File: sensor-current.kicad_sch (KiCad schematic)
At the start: 0 parts

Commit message: Adding I2C bus to circuit
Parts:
- added U8: INA260, Package_SO:TSSOP-16_4.4x5mm_P0.65mm, symbol Sensor:INA260
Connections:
- new net: U8.1 (IN+), U8.2 (IN+), U8.3 (IN+)
- new net: U8.14 (IN-), U8.15 (IN-), U8.16 (IN-)
- new net GND: U8.11 (GND), U8.6 (GND)
- new net I2C.SCL: U8.9 (SCL)
- new net I2C.SDA: U8.8 (SDA)
- no-connect marks 0 -> 3
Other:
- note added: "Where to connect the INA to? BATT VBUS lines"
- note added: "n/c"

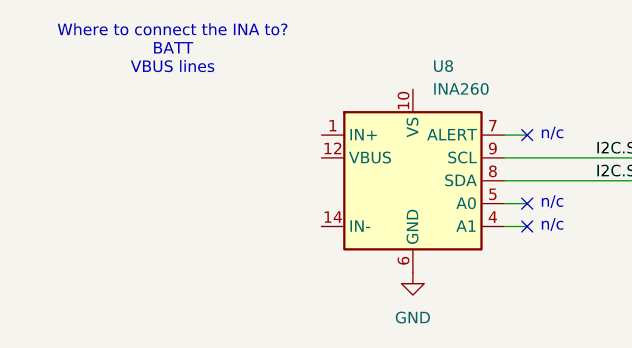
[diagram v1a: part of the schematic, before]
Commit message: Adding symbols information
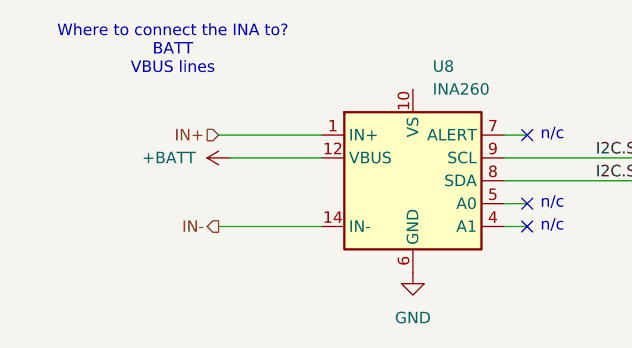
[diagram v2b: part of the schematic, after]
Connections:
- net IN+: now reaches U8.1 (IN+), U8.2 (IN+), U8.3 (IN+)
- net +BATT: now reaches U8.12 (VBUS)
- net IN-: now reaches U8.14 (IN-), U8.15 (IN-), U8.16 (IN-)
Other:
- company: (none) -> catbranchman
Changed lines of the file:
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@@
 	(generator_version "8.0")
 	(paper "A4")
+	(title_block
+		(company "catbranchman")
+		(comment 1 "Electrical Engineering Department")
+		(comment 2 "EE 156 / Stanford University")
+		(comment 3 "Flight Club, W6YX, Endurance")
+	)
 	(no_connect
 		(at 163.83 95.25)
@@
 		)
 	)
+	(wire
+		(pts
+			(xy 129.54 105.41) (xy 140.97 105.41)
+		)
+		(stroke
+			(width 0)
+			(type default)
+		)
+	)
 	(bus
 		(pts
@@
 	(wire
 		(pts
+			(xy 130.81 97.79) (xy 140.97 97.79)
+		)
+		(stroke
+			(width 0)
+			(type default)
+		)
+	)
+	(wire
+		(pts
 			(xy 161.29 95.25) (xy 163.83 95.25)
 		)
@@
 		(pts
 			(xy 161.29 105.41) (xy 163.83 105.41)
+		)
+		(stroke
+			(width 0)
+			(type default)
+		)
+	)
+	(wire
+		(pts
+			(xy 129.54 95.25) (xy 140.97 95.25)
 		)
 		(stroke
@@
 		)
 	)
+	(hierarchical_label "IN-"
+		(shape output)
+		(at 129.54 105.41 180)
+		(fields_autoplaced yes)
+		(effects
+			(font
+				(size 1.27 1.27)
+			)
+			(justify right)
+		)
+	)
+	(hierarchical_label "IN+"
+		(shape input)
+		(at 129.54 95.25 180)
+		(fields_autoplaced yes)
+		(effects
+			(font
+				(size 1.27 1.27)
+			)
+			(justify right)
+		)
+	)
+	(symbol
+		(lib_id "power:+BATT")
+		(at 130.81 97.79 90)
+		(unit 1)
+		(exclude_from_sim no)
+		(in_bom yes)
+		(on_board yes)
+		(dnp no)
+		(fields_autoplaced yes)
+		(property "Reference" "#PWR053"
+			(at 134.62 97.79 0)
+			(effects
+				(font
+					(size 1.27 1.27)
+				)
+				(hide yes)
+			)
+		)
+		(property "Value" "+BATT"
+			(at 127 97.7899 90)
+			(effects
+				(font
+					(size 1.27 1.27)
+				)
+				(justify left)
+			)
+		)
+		(property "Footprint" ""
+			(at 130.81 97.79 0)
+			(effects
+				(font
+					(size 1.27 1.27)
+				)
+				(hide yes)
+			)
+		)
+		(property "Datasheet" ""
+			(at 130.81 97.79 0)
+			(effects
+				(font
+					(size 1.27 1.27)
+				)
+				(hide yes)
+			)
+		)
+		(property "Description" "Power symbol creates a global label with name \"+BATT\""
+			(at 130.81 97.79 0)
+			(effects
+				(font
+					(size 1.27 1.27)
+				)
+				(hide yes)
+			)
+		)
+		(pin "1"
+		)
+		(instances
+			(project "roamer"
+				(path "/1c59de6a-87fe-4223-8898-4b0383164a31/7697eacc-831c-4a5e-b109-0bbe6f3888c4"
+					(reference "#PWR053")
+					(unit 1)
+				)
+			)
+		)
+	)

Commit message: Adding rest of schematic
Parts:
- U8: Mfr (none) -> Texas Instruments; Mfr P/N (none) -> INA260AIPWR; Supplier_1 (none) -> Digikey; Supplier_1 P/N (none) -> 296-47777-1-ND; Supplier_1 Price @ Qty (none) -> $2.85475; Supplier_1 Unit Price (none) -> $5.43000
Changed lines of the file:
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@@
 			)
 		)
-		(property "Description" "Current/power/voltage monitor with Integrated 2mΩ Shunt Resistor, 2.7V - 5.5V, I2C, TSSOP-16"
+		(property "Description" "Current Monitor Regulator High/Low-Side 10mA 16-TSSOP"
 			(at 151.13 100.33 0)
 			(effects
+				(font
+					(size 1.27 1.27)
+				)
+				(hide yes)
+			)
+		)
+		(property "Mfr" "Texas Instruments"
+			(at 151.13 100.33 0)
+			(effects
+				(font
+					(size 1.27 1.27)
+				)
+				(hide yes)
+			)
+		)
+		(property "Mfr P/N" "INA260AIPWR"
+			(at 151.13 100.33 0)
+			(effects
+				(font
+					(size 1.27 1.27)
+				)
+				(hide yes)
+			)
+		)
+		(property "Supplier_1" "Digikey"
+			(at 151.13 100.33 0)
+			(effects
+				(font
+					(size 1.27 1.27)
+				)
+				(hide yes)
+			)
+		)
+		(property "Supplier_1 P/N" "296-47777-1-ND"
+			(at 151.13 100.33 0)
+			(effects
+				(font
+					(size 1.27 1.27)
+				)
+				(hide yes)
+			)
+		)
+		(property "Supplier_1 Unit Price" "$5.43000"
+			(at 151.13 100.33 0)
+			(effects
+				(font
+					(size 1.27 1.27)
+				)
+				(hide yes)
+			)
+		)
+		(property "Supplier_1 Price @ Qty" "$2.85475"
+			(at 151.13 100.33 0)
+			(effects
+				(font
+					(size 1.27 1.27)
+				)
+				(hide yes)
+			)
+		)
+		(property "Supplier_2" ""
+			(at 151.13 100.33 0)
+			(effects
+				(font
+					(size 1.27 1.27)
+				)
+				(hide yes)
+			)
+		)
+		(property "Supplier_2 P/N" ""
+			(at 151.13 100.33 0)
+			(effects
+				(font
+					(size 1.27 1.27)
+				)
+				(hide yes)
+			)
+		)
+		(property "Supplier_2 Unit Price" ""
+			(at 151.13 100.33 0)
+			(effects
+				(font
+					(size 1.27 1.27)
+				)
+				(hide yes)
+			)
+		)
+		(property "Supplier_2 Price @ Qty" ""
+			(at 151.13 100.33 0)
+			(effects

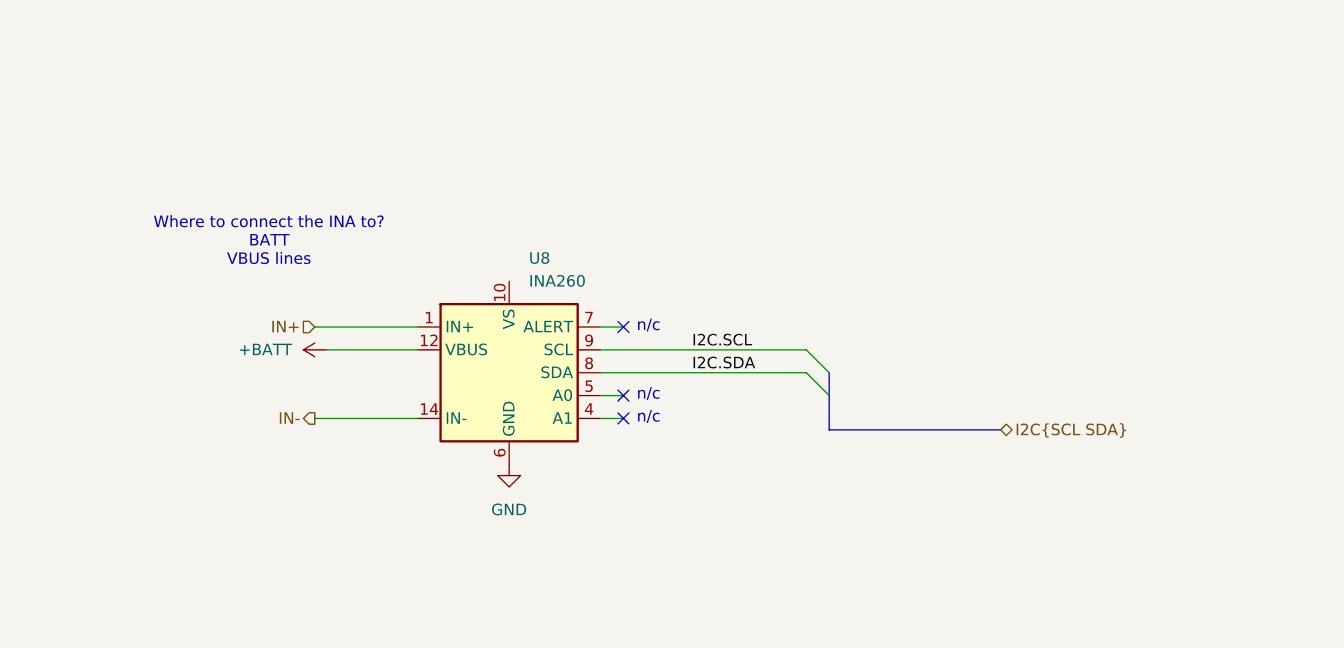
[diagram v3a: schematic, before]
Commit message: Spamming 0 ohm resistors
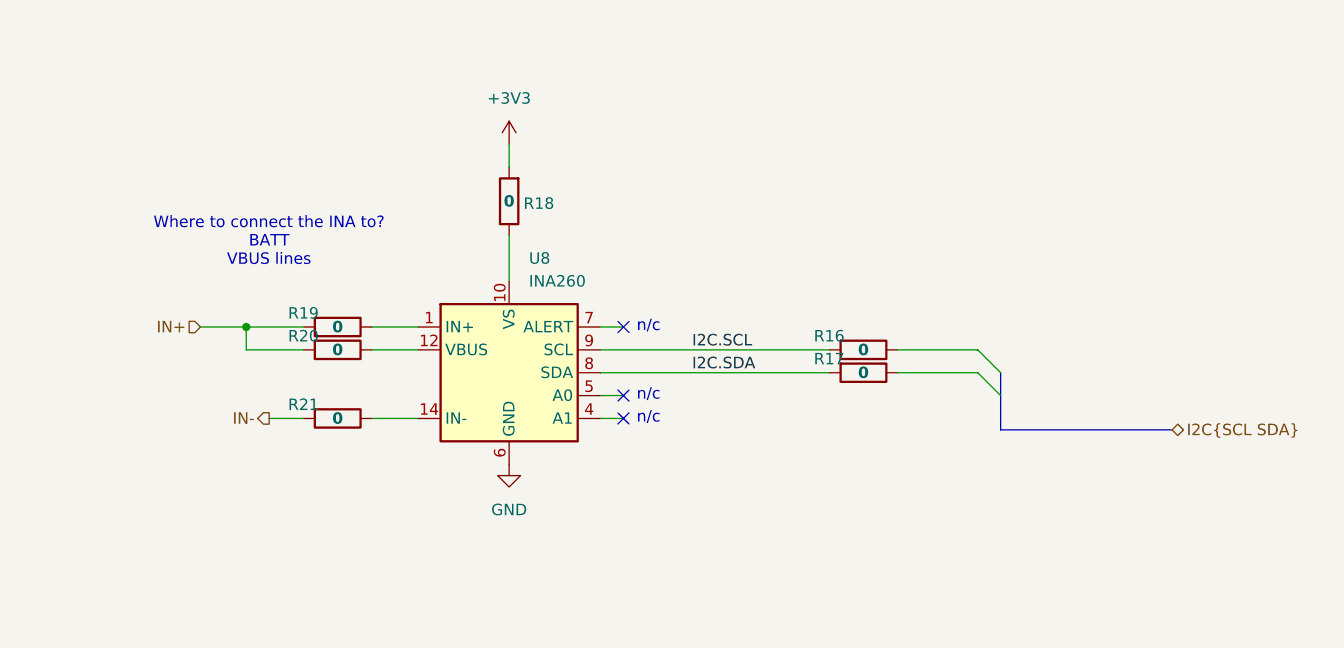
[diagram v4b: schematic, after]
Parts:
- added R16, R17, R18, R19, R20, R21: 0, Resistor_SMD:R_0603_1608Metric, symbol Device:R
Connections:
- net I2C.SCL: now also R16.2
- net I2C.SDA: now also R17.2
- net IN+: now also R19.2, R20.2; no longer U8.1 (IN+), U8.2 (IN+), U8.3 (IN+)
- net IN-: now also R21.2; no longer U8.14 (IN-), U8.15 (IN-), U8.16 (IN-)
- net at U8.10 (VS): now also R18.1
- net +BATT: no longer names the net of U8.12 (VBUS)
- net +BATT: now also R20.1
- new net: R19.1, U8.1 (IN+), U8.2 (IN+), U8.3 (IN+)
- new net: R21.1, U8.14 (IN-), U8.15 (IN-), U8.16 (IN-)
- new net +3V3: R18.2
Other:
- title: (none) -> Sensor - Current

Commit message: Adding more 0 ohm resistors and pullups for I2C lines
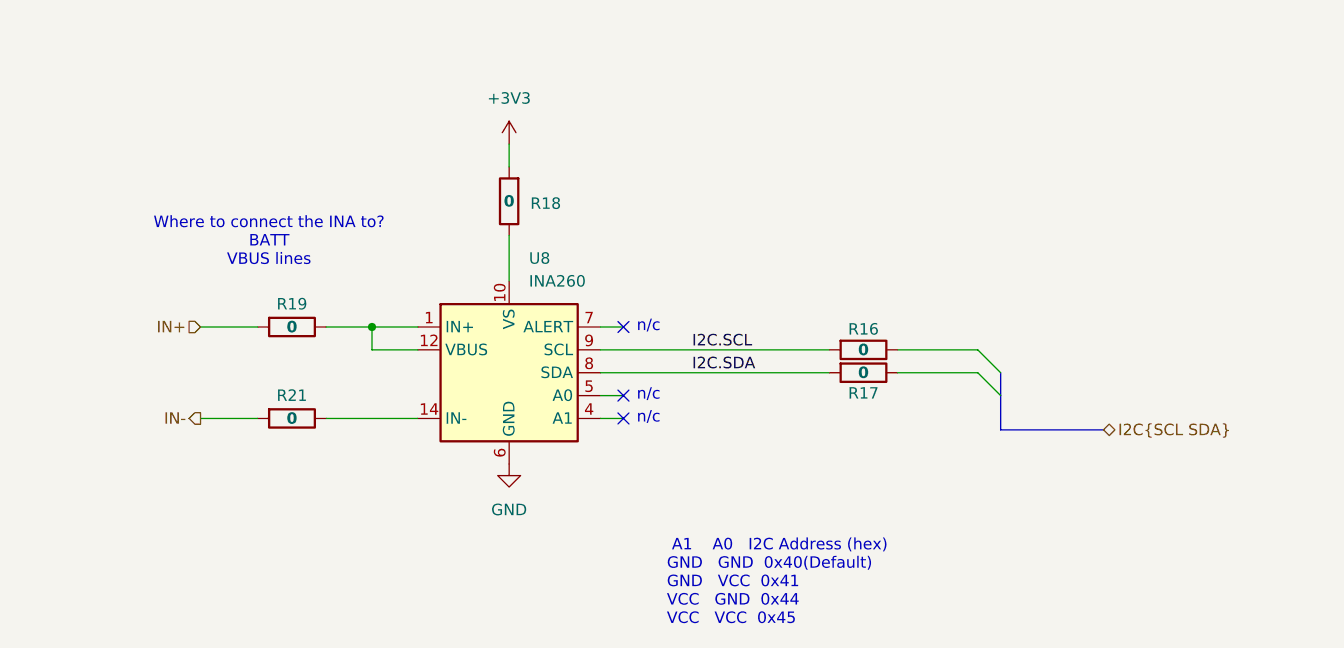
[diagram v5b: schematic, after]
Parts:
- removed R20: 0, Resistor_SMD:R_0603_1608Metric, symbol Device:R
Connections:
- net at R19.1, U8.1 (IN+), U8.2 (IN+)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: now also U8.12 (VBUS)
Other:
- note added: "A1 A0 I2C Address (hex) GND GND 0x40(Default) GND VCC 0x41 VCC GND 0x44 VCC VCC 0x45"
- moved on the sheet: R19, R21

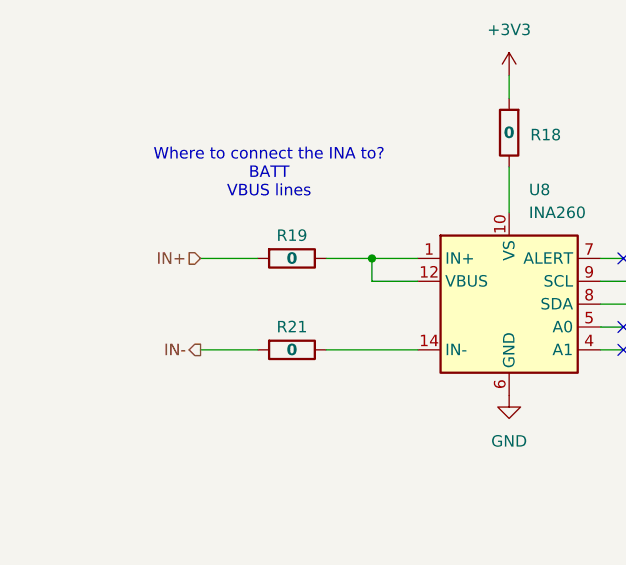
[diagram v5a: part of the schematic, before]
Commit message: Adding testpoints to I2C, SPI, and signals
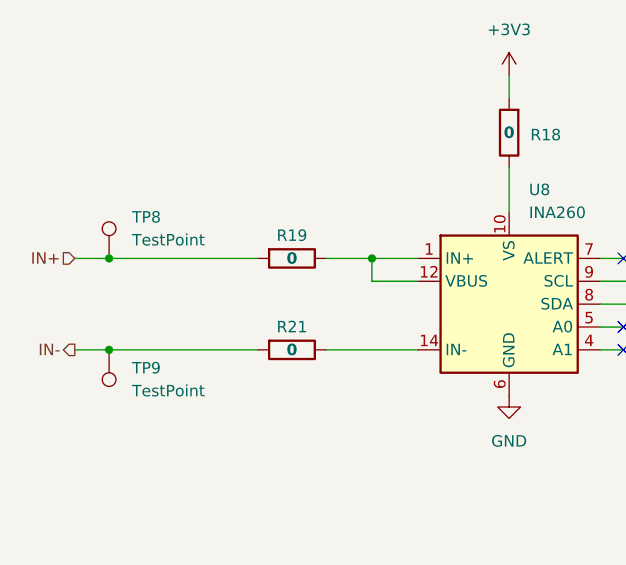
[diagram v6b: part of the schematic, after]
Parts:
- added TP8, TP9: TestPoint, TestPoint:TestPoint_Loop_D2.50mm_Drill1.0mm, symbol Connector:TestPoint
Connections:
- net IN+: now also TP8.1
- net IN-: now also TP9.1
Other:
- note removed: "Where to connect the INA to? BATT VBUS lines"

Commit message: Fixing lots of ERC errors
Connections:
- net I2C.SCL: now also R16.1; no longer R16.2, U8.9 (SCL)
- net I2C.SDA: now also R17.1; no longer R17.2, U8.8 (SDA)
- new net: R16.2, U8.9 (SCL)
- new net: R17.2, U8.8 (SDA)
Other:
- moved on the sheet: R16, R17
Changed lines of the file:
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@@
+	)
+	(junction
+		(at 151.13 87.63)
+		(diameter 0)
+		(color 0 0 0 0)
 	)
 	(junction
@@
 	)
 	(bus_entry
-		(at 203.2 97.79)
+		(at 191.77 97.79)
 		(size 2.54 2.54)
 		(stroke
@@
 	)
 	(bus_entry
-		(at 203.2 100.33)
+		(at 191.77 100.33)
 		(size 2.54 2.54)
 		(stroke
@@
 	(wire
 		(pts
-			(xy 151.13 85.09) (xy 151.13 90.17)
+			(xy 151.13 85.09) (xy 151.13 87.63)
 		)
 		(stroke
@@
 	(bus
 		(pts
-			(xy 205.74 100.33) (xy 205.74 102.87)
+			(xy 194.31 100.33) (xy 194.31 102.87)
 		)
 		(stroke
@@
 	(wire
 		(pts
-			(xy 194.31 100.33) (xy 203.2 100.33)
+			(xy 177.8 100.33) (xy 191.77 100.33)
 		)
 		(stroke
@@
 	(wire
 		(pts
-			(xy 161.29 100.33) (xy 186.69 100.33)
-		)
-		(stroke
-			(width 0)
-			(type default)
-		)
-	)
-	(wire
-		(pts
-			(xy 161.29 97.79) (xy 186.69 97.79)
+			(xy 161.29 100.33) (xy 170.18 100.33)
+		)
+		(stroke
+			(width 0)
+			(type default)
+		)
+	)
+	(wire
+		(pts
+			(xy 161.29 97.79) (xy 170.18 97.79)
 		)
 		(stroke
@@
 	(wire
 		(pts
-			(xy 194.31 97.79) (xy 203.2 97.79)
+			(xy 177.8 97.79) (xy 191.77 97.79)
 		)
 		(stroke
@@
 	(bus
 		(pts
-			(xy 205.74 102.87) (xy 205.74 106.68)
+			(xy 194.31 102.87) (xy 194.31 106.68)
+		)
+		(stroke
+			(width 0)
+			(type default)
+		)
+	)
+	(wire
+		(pts
+			(xy 151.13 87.63) (xy 151.13 90.17)
 		)
 		(stroke
@@
 	(bus
 		(pts
-			(xy 205.74 106.68) (xy 217.17 106.68)
+			(xy 194.31 106.68) (xy 205.74 106.68)
 		)
 		(stroke
@@
 	)
 	(label "I2C.SDA"
-		(at 171.45 100.33 0)
+		(at 180.34 100.33 0)
 		(fields_autoplaced yes)
 		(effects
@@
 	)
 	(label "I2C.SCL"
-		(at 171.45 97.79 0)
+		(at 180.34 97.79 0)
 		(fields_autoplaced yes)
 		(effects
@@
 	(hierarchical_label "I2C{SCL SDA}"
 		(shape bidirectional)
-		(at 217.17 106.68 0)
+		(at 205.74 106.68 0)
 		(fields_autoplaced yes)
 		(effects
@@
 	(symbol
 		(lib_id "Device:R")
-		(at 190.5 97.79 270)
+		(at 173.99 97.79 270)
 		(unit 1)
 		(exclude_from_sim no)
@@
 		(dnp no)
 		(property "Reference" "R16"
-			(at 190.5 95.504 90)
+			(at 173.99 95.504 90)
 			(effects
 				(font
@@
 		)
 		(property "Value" "0"
-			(at 190.5 97.79 90)
+			(at 173.99 97.79 90)
 			(effects
 				(font
@@
 		)
 		(property "Footprint" "Resistor_SMD:R_0603_1608Metric"
-			(at 190.5 96.012 90)
+			(at 173.99 96.012 90)
 			(effects
 				(font
@@
 		)
 		(property "Datasheet" "Datasheet"
-			(at 190.5 97.79 0)
+			(at 173.99 97.79 0)
 			(effects
 				(font
@@
 		)
 		(property "Description" "Resistor"
-			(at 190.5 97.79 0)
+			(at 173.99 97.79 0)
 			(effects
 				(font
@@
 		)
 		(property "Mfr" "YAGEO"
-			(at 190.5 97.79 0)
+			(at 173.99 97.79 0)
 			(effects
 				(font
@@
 		)
 		(property "Mfr P/N" "RC0603JR-070RL"
-			(at 190.5 97.79 0)
+			(at 173.99 97.79 0)
 			(effects
 				(font
@@
 		)
 		(property "Supplier_1" "Digikey"
-			(at 190.5 97.79 0)
+			(at 173.99 97.79 0)
 			(effects
 				(font
@@
 		)
 		(property "Supplier_1 P/N" "311-0.0GRCT-ND"
-			(at 190.5 97.79 0)
+			(at 173.99 97.79 0)
 			(effects
 				(font
@@
 		)
 		(property "Supplier_1 Unit Price" "$0.10000 "
-			(at 190.5 97.79 0)
+			(at 173.99 97.79 0)
 			(effects
 				(font
@@
 		)
 		(property "Supplier_1 Price @ Qty" "$0.00304 "
-			(at 190.5 97.79 0)
+			(at 173.99 97.79 0)
 			(effects
 				(font
@@
 		)
 		(property "Supplier_2" ""
-			(at 190.5 97.79 0)
+			(at 173.99 97.79 0)
 			(effects
 				(font
@@
 		)
 		(property "Supplier_2 P/N" ""
-			(at 190.5 97.79 0)
+			(at 173.99 97.79 0)
 			(effects
 				(font
@@
 		)
 		(property "Supplier_2 Unit Price" ""
-			(at 190.5 97.79 0)
+			(at 173.99 97.79 0)
 			(effects
 				(font
@@
 		)
 		(property "Supplier_2 Price @ Qty" ""
-			(at 190.5 97.79 0)
+			(at 173.99 97.79 0)
 			(effects
 				(font
@@
 	(symbol
 		(lib_id "Device:R")
-		(at 190.5 100.33 270)
+		(at 173.99 100.33 270)
 		(unit 1)
 		(exclude_from_sim no)
@@
 		(dnp no)
 		(property "Reference" "R17"
-			(at 190.5 102.616 90)
+			(at 173.99 102.616 90)
 			(effects
 				(font
@@
 		)
 		(property "Value" "0"
-			(at 190.5 100.33 90)
+			(at 173.99 100.33 90)
 			(effects
 				(font
@@
 		)
 		(property "Footprint" "Resistor_SMD:R_0603_1608Metric"
-			(at 190.5 98.552 90)
+			(at 173.99 98.552 90)
 			(effects
 				(font
@@
 		)
 		(property "Datasheet" "Datasheet"
-			(at 190.5 100.33 0)
+			(at 173.99 100.33 0)
 			(effects
 				(font
@@
 		)
 		(property "Description" "Resistor"
-			(at 190.5 100.33 0)
+			(at 173.99 100.33 0)
 			(effects
 				(font
@@
 		)
 		(property "Mfr" "YAGEO"
-			(at 190.5 100.33 0)
+			(at 173.99 100.33 0)
 			(effects
 				(font
@@
 		)
 		(property "Mfr P/N" "RC0603JR-070RL"
-			(at 190.5 100.33 0)
+			(at 173.99 100.33 0)
 			(effects
 				(font
@@
 		)
 		(property "Supplier_1" "Digikey"
-			(at 190.5 100.33 0)
+			(at 173.99 100.33 0)
 			(effects
 				(font
@@
 		)
 		(property "Supplier_1 P/N" "311-0.0GRCT-ND"
-			(at 190.5 100.33 0)
+			(at 173.99 100.33 0)
 			(effects
 				(font
@@
 		)
 		(property "Supplier_1 Unit Price" "$0.10000 "
-			(at 190.5 100.33 0)
+			(at 173.99 100.33 0)
 			(effects
 				(font
@@
 		)
 		(property "Supplier_1 Price @ Qty" "$0.00304 "
-			(at 190.5 100.33 0)
+			(at 173.99 100.33 0)
 			(effects
 				(font
@@
 		)
 		(property "Supplier_2" ""
-			(at 190.5 100.33 0)
+			(at 173.99 100.33 0)
 			(effects
 				(font
@@
 		)
 		(property "Supplier_2 P/N" ""
-			(at 190.5 100.33 0)
+			(at 173.99 100.33 0)
 			(effects
 				(font
@@
 		)
 		(property "Supplier_2 Unit Price" ""
-			(at 190.5 100.33 0)
+			(at 173.99 100.33 0)
 			(effects
 				(font
@@
 		)
 		(property "Supplier_2 Price @ Qty" ""
-			(at 190.5 100.33 0)
+			(at 173.99 100.33 0)
 			(effects
 				(font
@@
 					(unit 1)
 				)
+			)
+		)
+	)
+	(symbol
+		(lib_id "power:PWR_FLAG")
+		(at 151.13 87.63 90)
+		(unit 1)
+		(exclude_from_sim no)
+		(in_bom yes)
+		(on_board yes)
+		(dnp no)
+		(fields_autoplaced yes)
+		(property "Reference" "#FLG07"
+			(at 149.225 87.63 0)
+			(effects
+				(font
+					(size 1.27 1.27)
+				)
+				(hide yes)
+			)
+		)
+		(property "Value" "PWR_FLAG"
+			(at 147.32 87.6299 90)
+			(effects
+				(font
+					(size 1.27 1.27)
+				)
+				(justify left)
+			)
+		)
+		(property "Footprint" ""
+			(at 151.13 87.63 0)
+			(effects
+				(font
+					(size 1.27 1.27)
+				)
+				(hide yes)
+			)
+		)
+		(property "Datasheet" "~"
+			(at 151.13 87.63 0)
+			(effects
+				(font
+					(size 1.27 1.27)
+				)
+				(hide yes)
+			)
+		)
+		(property "Description" "Special symbol for telling ERC where power comes from"
+			(at 151.13 87.63 0)
+			(effects
+				(font
+					(size 1.27 1.27)
+				)
+				(hide yes)
+			)
+		)
+		(pin "1"
+		)
+		(instances
+			(project "roamer"
+				(path "/1c59de6a-87fe-4223-8898-4b0383164a31/7697eacc-831c-4a5e-b109-0bbe6f3888c4"
+					(reference "#FLG07")
+					(unit 1)
+				)

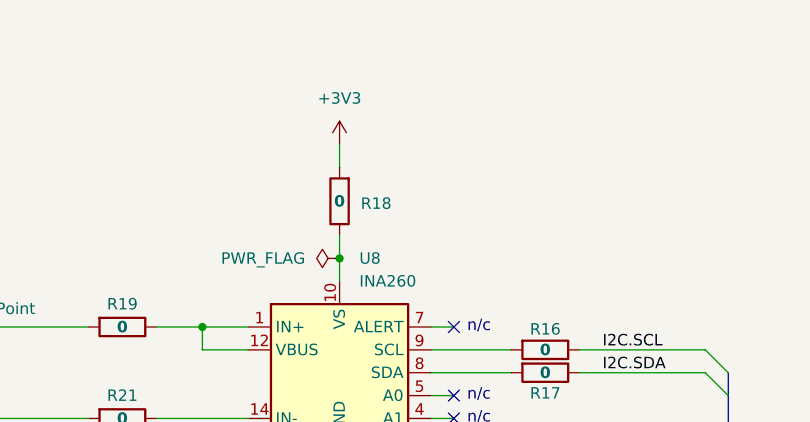
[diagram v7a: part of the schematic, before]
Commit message: Added mounting holes
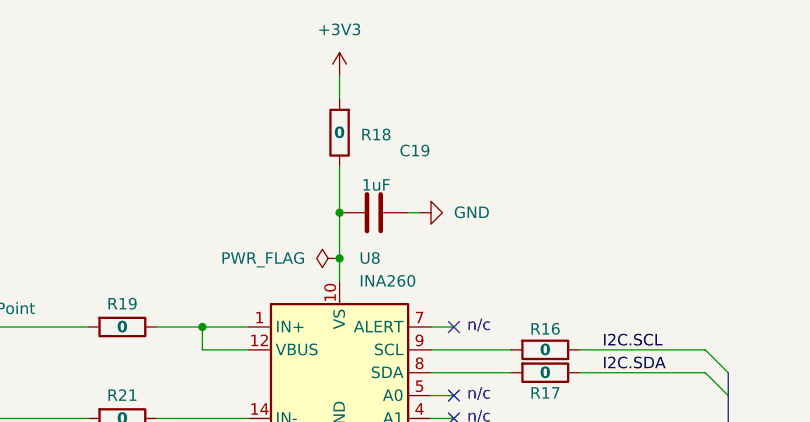
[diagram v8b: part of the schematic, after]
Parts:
- added C19: 1uF, Capacitor_SMD:C_0603_1608Metric, symbol Device:C
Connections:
- net GND: now also C19.2
- net at R18.1, U8.10 (VS): now also C19.1
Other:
- moved on the sheet: R18
